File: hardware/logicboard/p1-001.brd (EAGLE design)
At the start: 91 x 57 mm, 36 parts, among them J7 DIN5, K1A G5V1, K1B G5V1, K1C G5V1, T1A 2SC1815, T1B 2SC1815, T1C 2SC1815

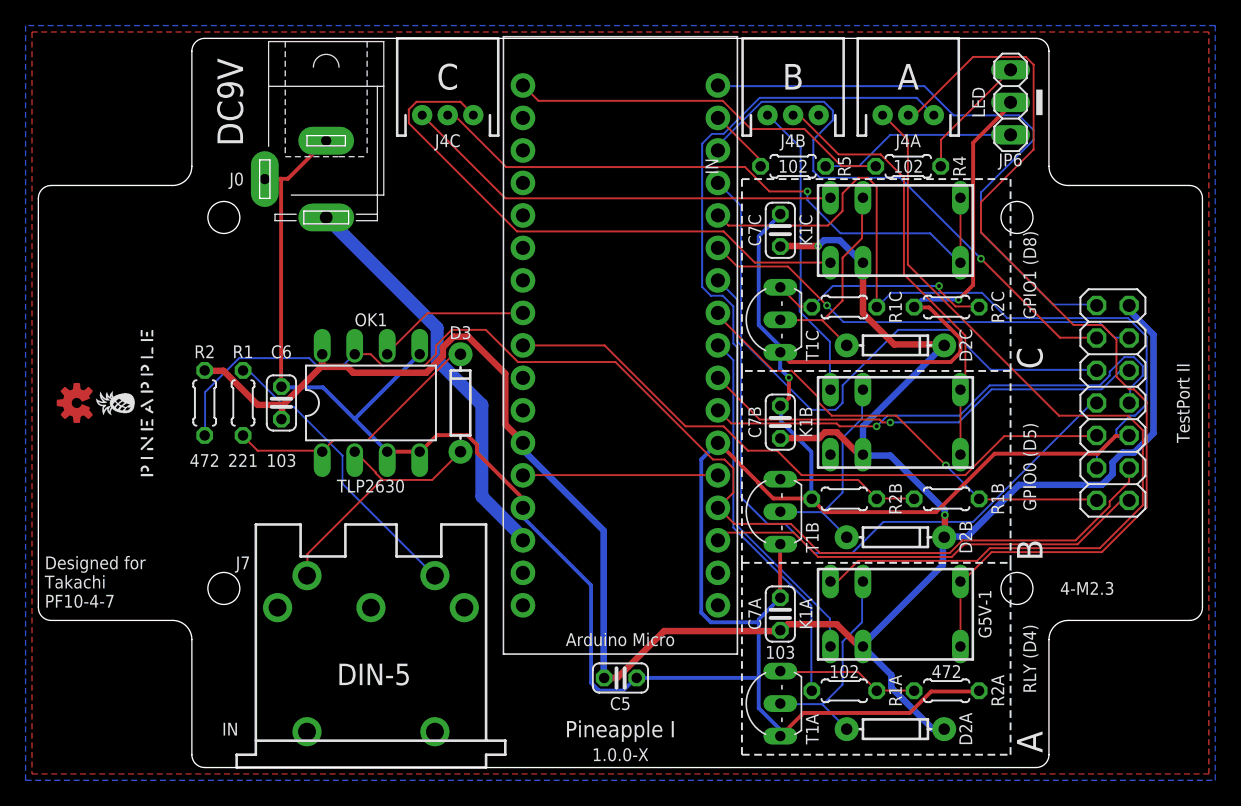
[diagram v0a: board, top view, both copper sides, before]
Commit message: Fixed signaling error.
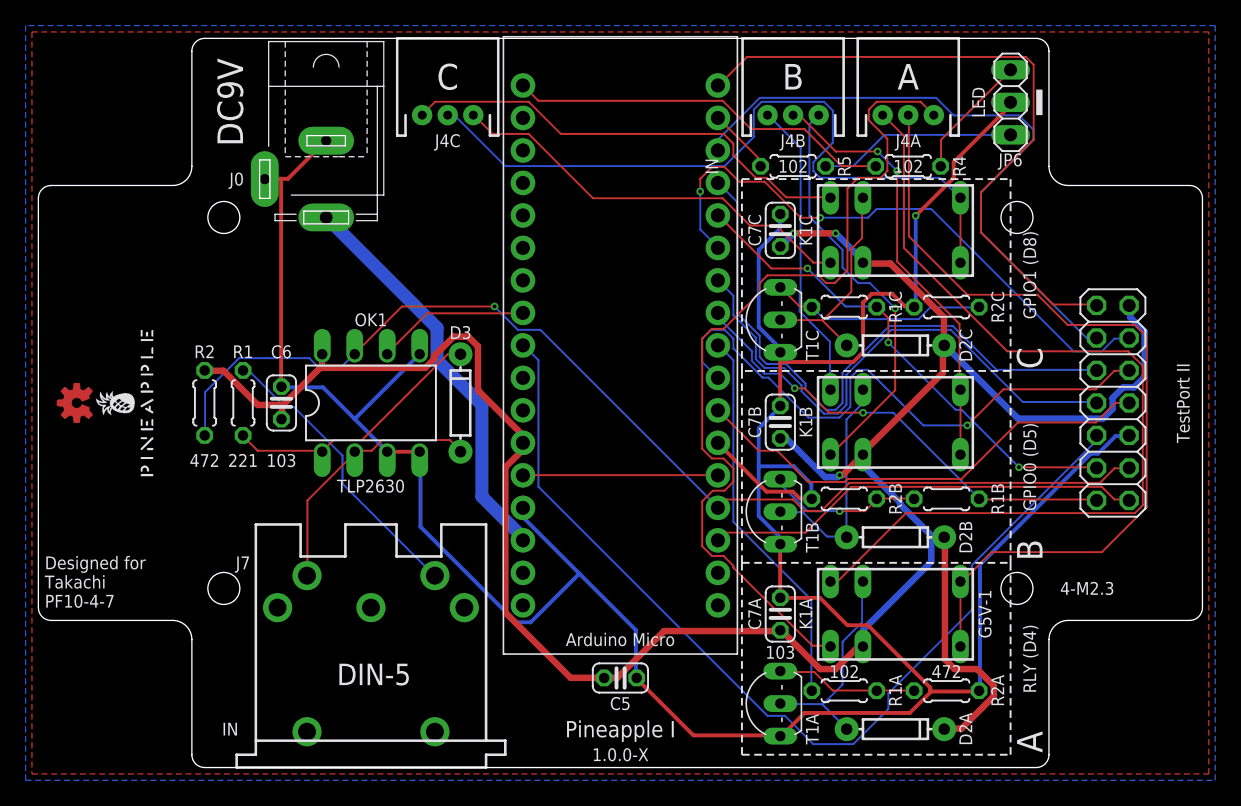
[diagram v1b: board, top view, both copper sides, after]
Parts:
- J0: value (none) -> DC9V
- J4A: value (none) -> RLYOUT-A
- J4B: value (none) -> RLYOUT-B
- J4C: value (none) -> RLYOUT-C
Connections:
- removed net RLYOUT3A: J4B.3
- net RLYOUT3B: now also J4B.3
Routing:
- net RLYOUT3B: track 0.00 -> 32.3 mm, vias 0 -> 1
- net THS: track 50.3 -> 76.5 mm
- net GPIO1: track 59.9 -> 38.9 mm, vias 0 -> 3
- net D7GATE: track 35.1 -> 46.9 mm, vias 1 -> 2
- net SCL: track 35.3 -> 47.0 mm
- net RLYOUT3C: track 44.3 -> 32.7 mm
- net RLYOUT2: track 77.2 -> 66.8 mm
- net DTCT0: track 52.2 -> 42.5 mm
- net VCC: track 180.1 -> 188.0 mm, vias 2 -> 3
- net RLYOUT2C: track 50.3 -> 58.2 mm, vias 1 -> 0
- net RX: track 93.7 -> 87.5 mm, vias 0 -> 1
- net DTCT2: track 44.0 -> 50.1 mm, vias 1 -> 0
- net DTCT3: track 47.2 -> 52.1 mm
- net RLYOUT3: track 64.1 -> 68.5 mm
- net GND: track 239.3 -> 235.7 mm, vias 2 -> 1
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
